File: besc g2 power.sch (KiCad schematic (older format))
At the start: 169 parts, among them J1 PHASE WIRE, J2 PHASE WIRE, J3 PHASE WIRE, J4 BUSBAR, J5 BUSBAR, J6 IN+, J7 IN-, Q1 IRF135B203, Q10 IRF135B203, Q11 IRF135B203, Q12 IRF135B203, Q13 IRF135B203, Q14 IRF135B203, Q15 IRF135B203, Q16 IRF135B203, Q17 IRF135B203, Q18 IRF135B203, Q19 IRF135B203, Q2 IRF135B203, Q20 IRF135B203, Q21 IRF135B203, Q22 IRF135B203, Q23 IRF135B203, Q24 IRF135B203, Q3 IRF135B203, Q4 IRF135B203, Q5 IRF135B203, Q6 IRF135B203, Q7 IRF135B203, Q8 IRF135B203, Q9 IRF135B203, U1 UCC21520DW, U2 UCC21520DW, U3 UCC21520DW, U4 INA240A1D, U5 INA240A1D, U6 INA240A1D

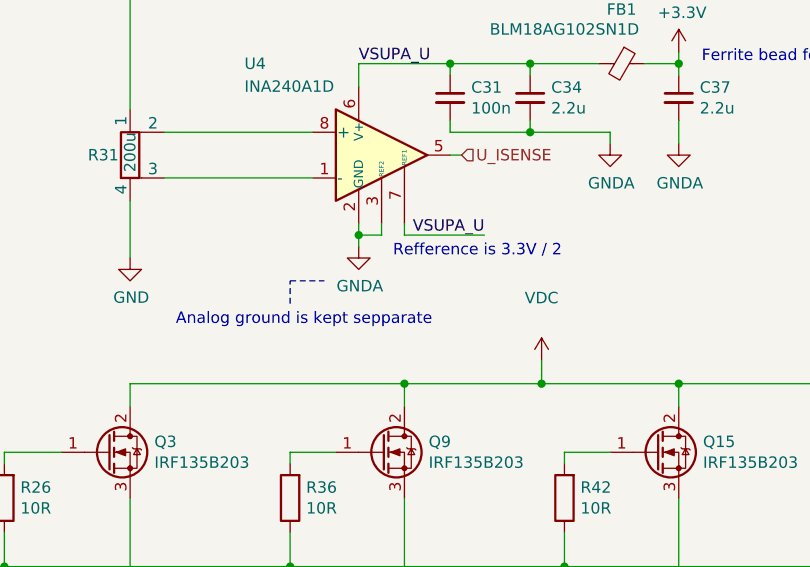
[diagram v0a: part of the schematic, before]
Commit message: Added brakes, i2c
Signed-off-by: manianac <manianac@gmail.com>
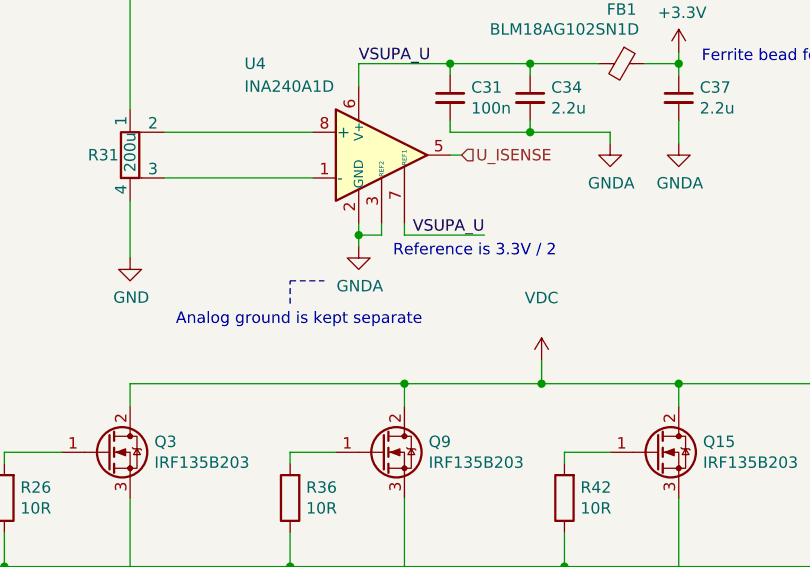
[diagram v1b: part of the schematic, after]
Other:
- note added: "Analog ground is kept separate"
- note added: "Reference is 3.3V / 2"
- note removed: "Analog ground is kept sepparate"
- note removed: "Refference is 3.3V / 2"
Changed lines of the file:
@@
 EESchema Schematic File Version 4
-LIBS:besc g2-cache
-EELAYER 29 0
+EELAYER 30 0
 EELAYER END
 $Descr A3 16535 11693
@@
 DT=10xR\nns / kOhm
 Text Notes 7000 4050 0    50   ~ 0
-Refference is 3.3V / 2
+Reference is 3.3V / 2
 Text Notes 8350 3200 0    50   ~ 0
 Ferrite bead for HF filtering
@@
 	1250 1550 1250 2000
 Text Notes 6050 4350 0    50   ~ 0
-Analog ground is kept sepparate
+Analog ground is kept separate
 Wire Notes Line
 	6550 4250 6550 4150
